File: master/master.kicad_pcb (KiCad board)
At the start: 2 copper layers, 480 x 20 mm, 12 parts

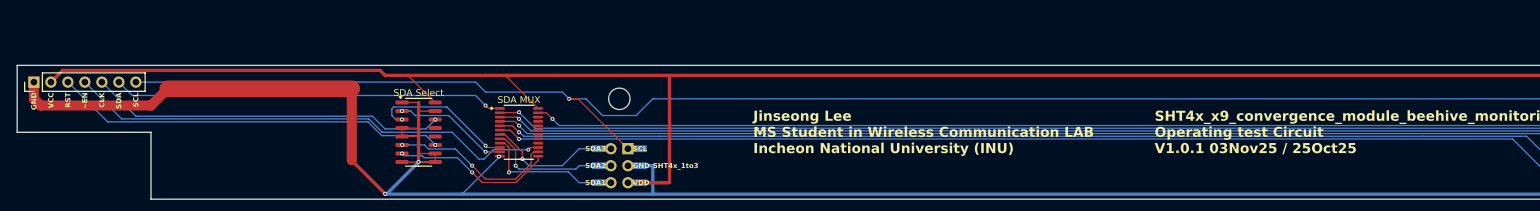
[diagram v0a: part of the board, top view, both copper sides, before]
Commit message: udpate to v1.1.0
udpate to v1.1.0
master : modify connector 2.54->1.25
slave : modify capacitor 0201->0402
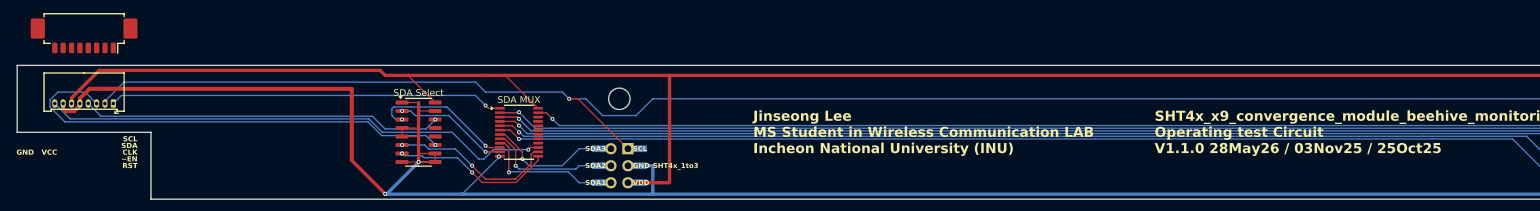
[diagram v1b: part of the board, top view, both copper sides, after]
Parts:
- removed the REF** at (62.5, 192.5)
- added REF**: Molex_PicoBlade_53261-0871_1x08-1MP_P1.25mm_Horizontal, Connector_Molex:Molex_PicoBlade_53261-0871_1x08-1MP_P1.25mm_Horizontal, F.Cu at (70.0, 185.0)
- added REF**: Molex_PicoBlade_53048-0810_1x08_P1.25mm_Horizontal, Connector_Molex:Molex_PicoBlade_53048-0810_1x08_P1.25mm_Horizontal, F.Cu at (74.4, 195.7)
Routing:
- net ~PL: track 58.8 -> 69.2 mm
- net SCL: track 405.6 -> 411.7 mm
- net gnd: track 475.2 -> 469.8 mm
- net ~EN: track 73.2 -> 76.4 mm
- net vcc: track 472.8 -> 471.6 mm
- net CP: track 53.3 -> 54.1 mm
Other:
- board text added: "SHT4x_x9_convergence_module_beehive_monitoring Operating test Circuit V1.1.0 28May26 / 03Nov25 / 25Oct25"
- board text removed: "SHT4x_x9_convergence_module_beehive_monitoring Operating test Circuit V1.0.1 03Nov25 / 25Oct25"
